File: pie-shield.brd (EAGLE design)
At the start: 35.1 x 25.2 mm, 20 parts, among them IC4 NRF24L01SMD, Q2 3.2X2.5CRYSTAL

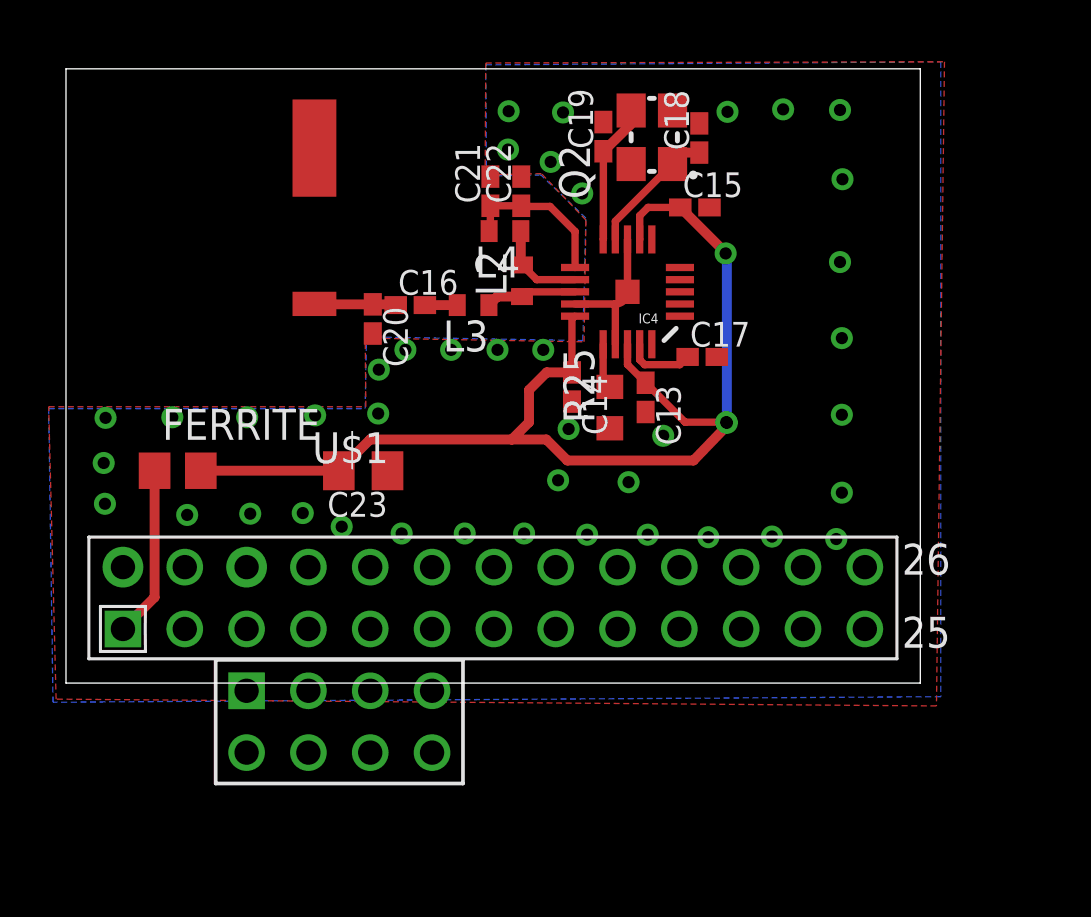
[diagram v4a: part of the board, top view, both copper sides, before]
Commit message: minified and dru tested
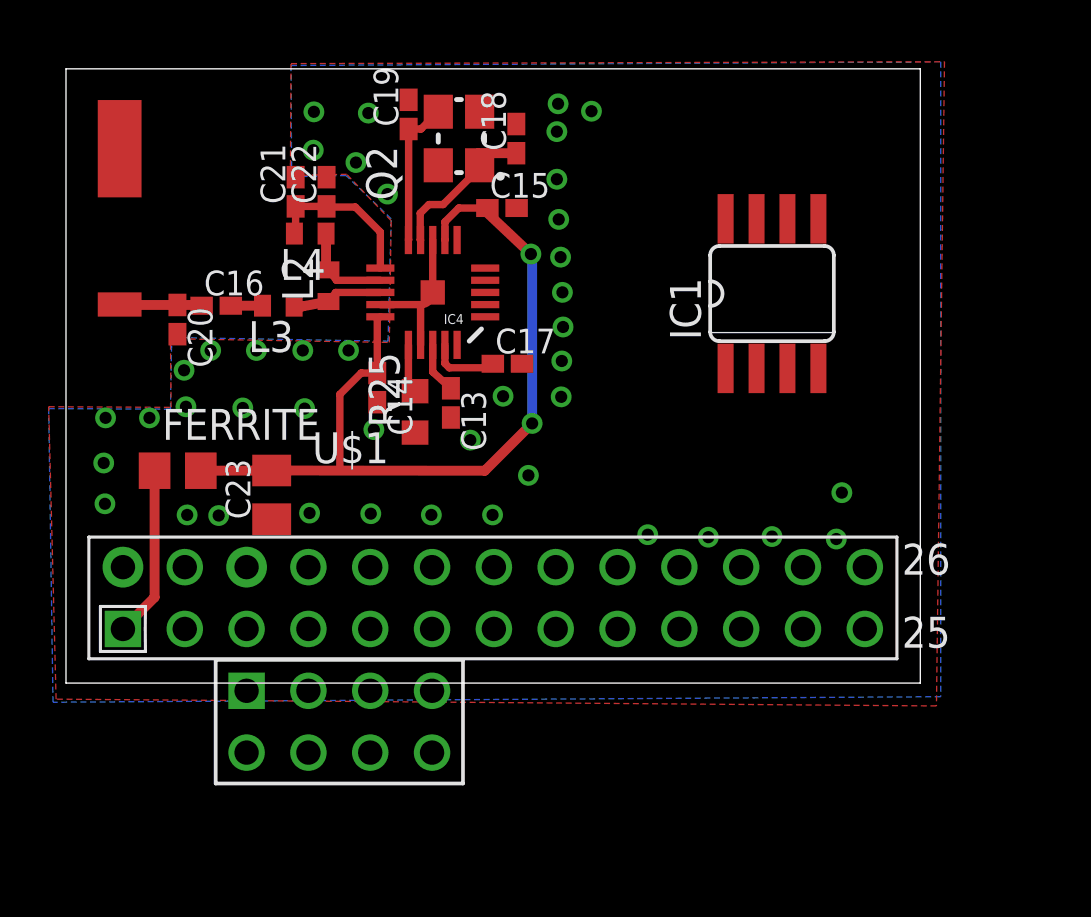
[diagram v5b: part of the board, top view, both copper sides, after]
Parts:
- added IC1: MAX481CSA, maxim:SO08
- moved C19 8.05 mm to (14.1, 25.0)
- moved C20 8.03 mm to (4.58, 16.6)
- moved C17 8.01 mm to (18.1, 14.8)
- moved C13 8.00 mm to (15.8, 13.2)
- moved R25 8.00 mm to (14.3, 12.8)
- moved L4 8.00 mm to (10.0, 20.1)
- moved C14 8.00 mm to (12.8, 13.8)
- moved C21 8.00 mm to (9.43, 21.9)
- moved ANT 8.00 mm to (2.21, 19.7)
- moved C22 8.00 mm to (10.7, 21.9)
- moved IC4 8.00 mm to (15.1, 17.7)
- moved L3 8.00 mm to (8.72, 17.2)
- moved C16 7.98 mm to (6.17, 17.2)
- moved L2 7.95 mm to (10.8, 18.0)
- moved Q2 7.92 mm to (16.1, 24.1)
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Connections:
- new net N$1: U$1.P1_25
- new net N$2: U$1.P1_26
- new net N$4: U$1.P1_24
- new net N$5: U$1.P1_22
- new net VCC: IC1.8
- net GND: now also IC1.5
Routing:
- net +3V3_RF: track 48.4 -> 39.1 mm, vias 3 -> 2
- net N$10: track 5.64 -> 6.51 mm
- net GND: vias 41 -> 42

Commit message: 1 square inch reached
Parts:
- removed IC1: MAX481CSA, maxim:SO08
- moved FERRITE 14.3 mm to (18.8, 8.98)
- moved C23 11.7 mm to (19.8, 12.0), turned to 270 degrees
- moved C15 10.1 mm to (28.0, 20.9)
- moved C17 10.1 mm to (28.3, 14.5)
- moved C21 10.1 mm to (19.6, 21.6)
- moved Q2 10.1 mm to (26.3, 23.7)
- moved C19 10.1 mm to (24.2, 24.7)
- moved C20 10.1 mm to (14.7, 16.3)
- moved C22 10.1 mm to (20.8, 21.6)
- moved IC4 10.1 mm to (25.2, 17.4)
- moved L2 10.1 mm to (20.9, 17.7)
- moved L3 10.1 mm to (18.9, 16.9)
- moved R25 10.1 mm to (24.5, 12.5)
- moved ANT 10.1 mm to (12.3, 19.4)
- moved C13 10.1 mm to (26.0, 12.9)
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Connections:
- removed net N$2: U$1.P1_26
- removed net N$5: U$1.P1_22
- removed net VCC: IC1.8
- net +3V3: now also U$1.P1_17; no longer U$1.P1_1
- net CE: now also U$1.P1_22
- net CSN: now also U$1.P1_24
- net GND: now also U$1.P1_25; no longer IC1.5
- net IRQ: now also U$1.P1_26
- net N$1: now also U$1.P1_15; no longer U$1.P1_25
- net N$3: now also U$1.P1_18; no longer U$1.P1_17
- net N$4: now also U$1.P1_16; no longer U$1.P1_24
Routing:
- net MOSI: track 0.00 -> 21.4 mm, vias 0 -> 1
- net MISO: track 0.00 -> 21.1 mm, vias 0 -> 1
- net IRQ: track 0.00 -> 19.3 mm
- net SCK: track 0.00 -> 17.5 mm
- net CSN: track 0.00 -> 13.1 mm
- net CE: track 0.00 -> 12.8 mm
- net +3V3: track 7.04 -> 8.24 mm
- net +3V3_RF: track 39.1 -> 38.6 mm
- net GND: vias 42 -> 32
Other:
- board size 35.1 x 25.2 mm -> 25 x 25.2 mm

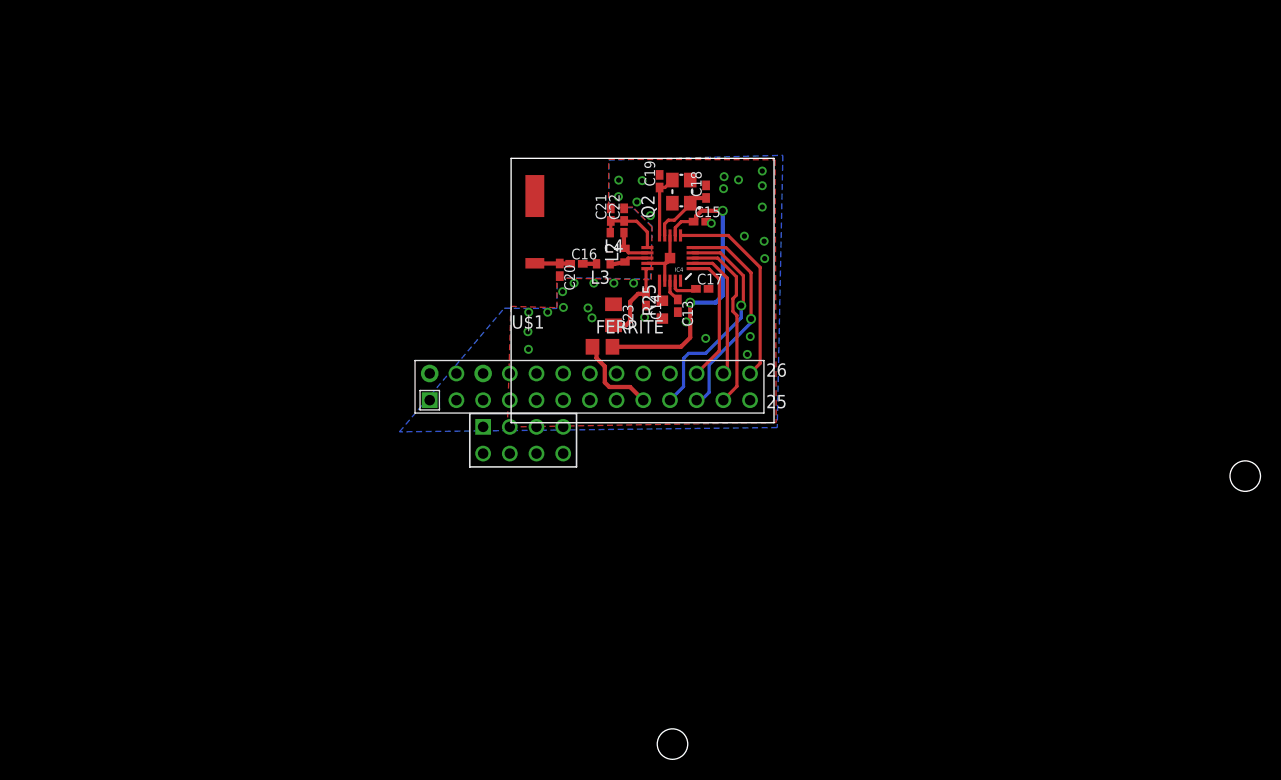
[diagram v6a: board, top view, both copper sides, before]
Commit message: fixed layout mirrored it
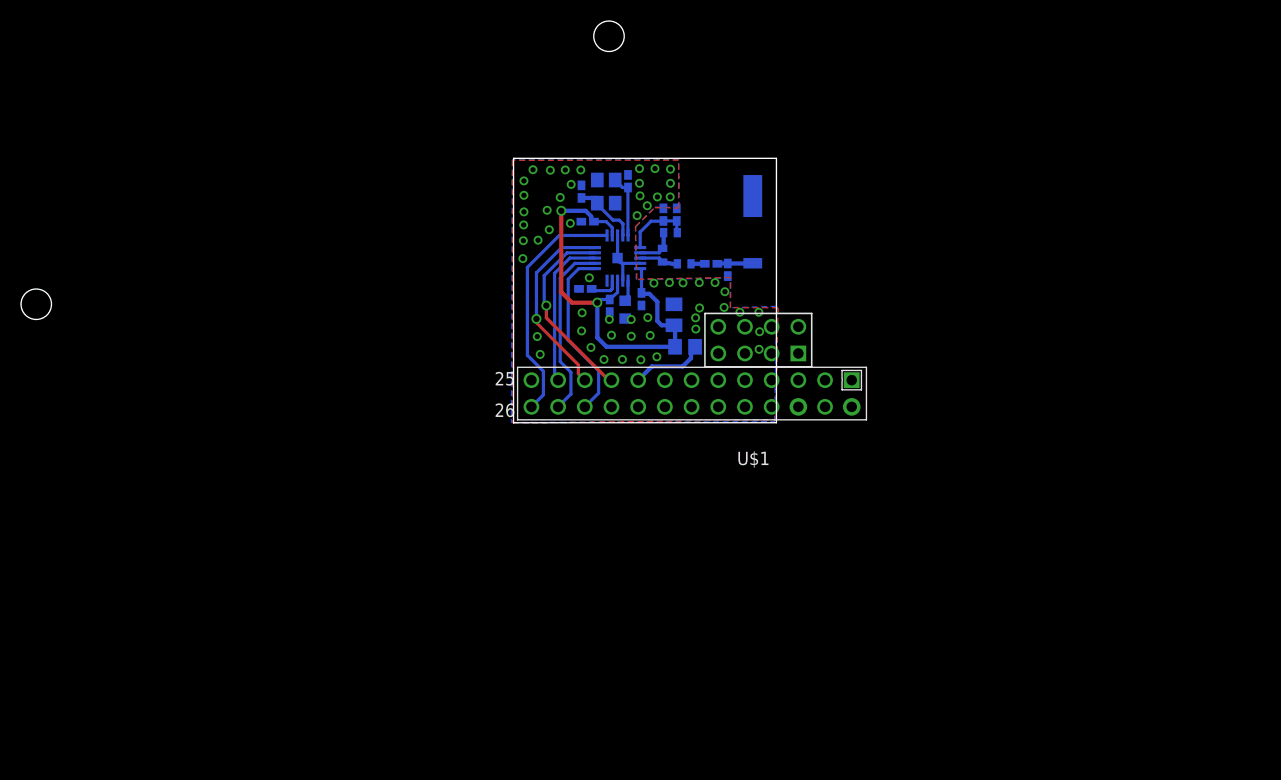
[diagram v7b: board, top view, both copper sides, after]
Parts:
- moved U$1 62.8 mm to (0.59, 27.4), turned to 180 degrees
- moved ANT 20.7 mm to (33.1, 19.4), flipped to the bottom
- moved C20 16.0 mm to (30.7, 16.3), flipped to the bottom
- moved C16 12.8 mm to (29.1, 16.9), flipped to the bottom
- moved C18 11.9 mm to (16.8, 23.7), flipped to the bottom
- moved C17 11.1 mm to (17.1, 14.5), flipped to the bottom
- moved C15 10.7 mm to (17.4, 20.9), flipped to the bottom
- moved FERRITE 7.86 mm to (26.6, 8.98), flipped to the bottom
- moved L3 7.70 mm to (26.6, 16.9), flipped to the bottom
- moved Q2 7.14 mm to (19.1, 23.7), flipped to the bottom
- moved C13 6.49 mm to (19.5, 12.9), flipped to the bottom
- moved C21 6.28 mm to (25.8, 21.6), flipped to the bottom
- moved C23 5.76 mm to (25.6, 12.0), flipped to the bottom
- moved L4 5.08 mm to (25.2, 19.8), flipped to the bottom
- moved IC4 4.99 mm to (20.2, 17.4), flipped to the bottom
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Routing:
- net CE: track 12.8 -> 16.9 mm
- net CSN: track 13.1 -> 17.1 mm
- net IRQ: track 19.3 -> 23.2 mm
- net +3V3_RF: track 38.6 -> 42.4 mm
- net MOSI: track 21.4 -> 18.5 mm
- net SCK: track 17.5 -> 14.7 mm
- net MISO: track 21.1 -> 18.7 mm
- net +3V3: track 8.24 -> 7.13 mm
- net GND: vias 32 -> 56

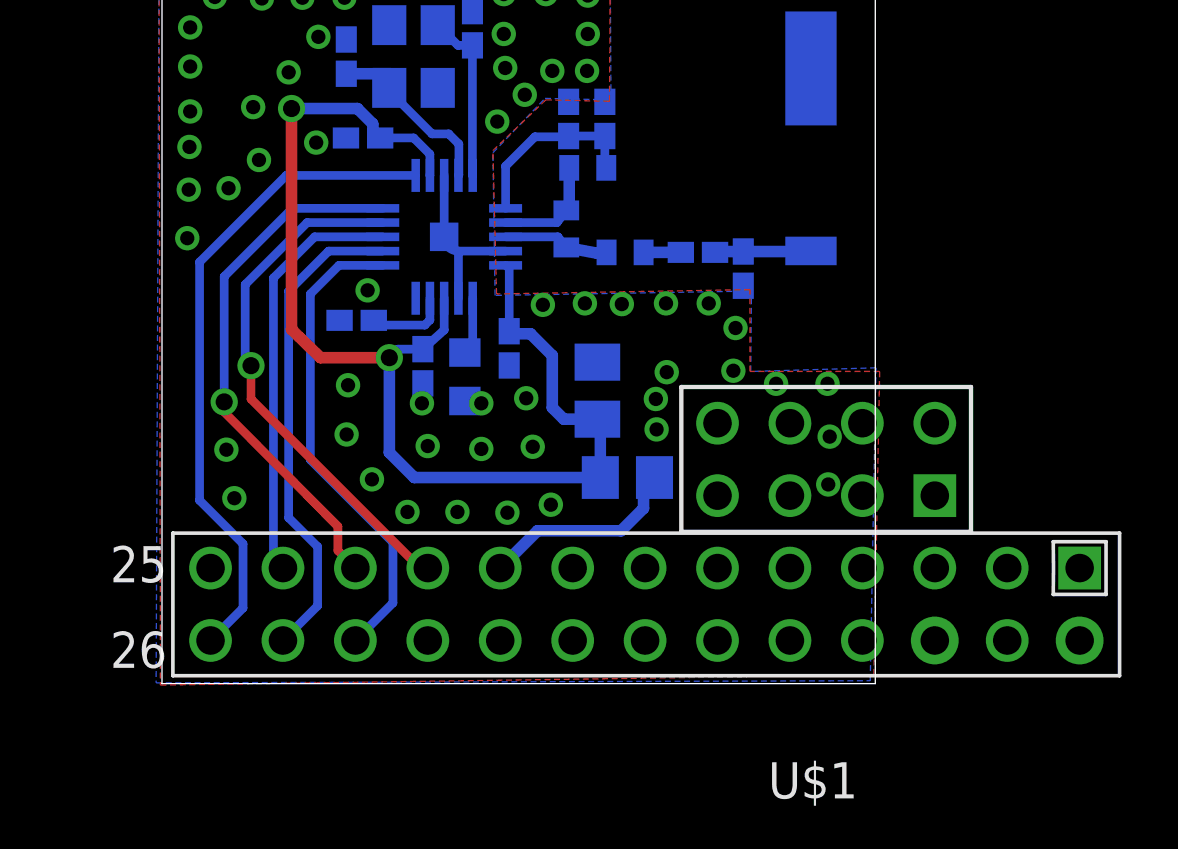
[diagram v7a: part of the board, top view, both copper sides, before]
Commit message: updated to smaller version of raspberry io
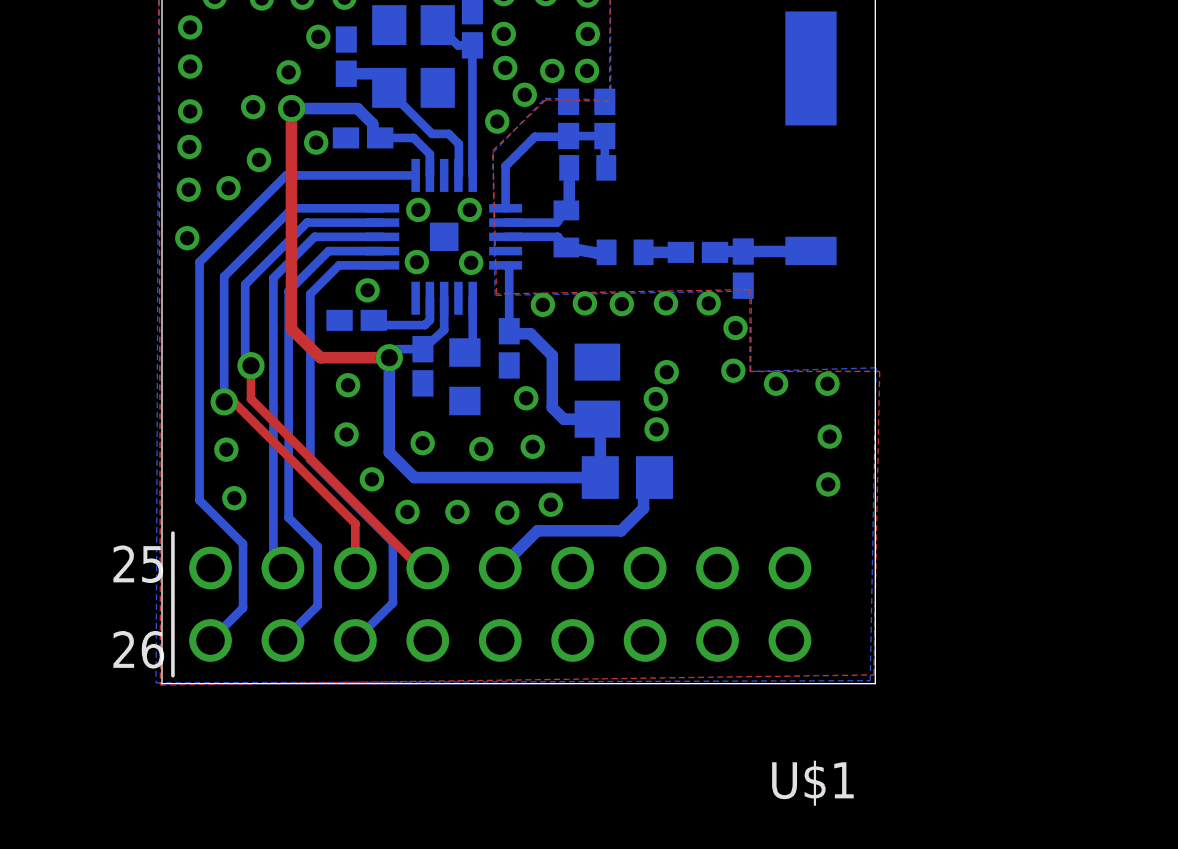
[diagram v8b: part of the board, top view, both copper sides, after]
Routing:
- net GND: track 6.17 -> 0.00 mm, vias 56 -> 58
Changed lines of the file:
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@@
 <layer number="27" name="tValues" color="7" fill="1" visible="yes" active="yes"/>
 <layer number="28" name="bValues" color="7" fill="1" visible="yes" active="yes"/>
-<layer number="29" name="tStop" color="7" fill="3" visible="no" active="yes"/>
-<layer number="30" name="bStop" color="7" fill="6" visible="no" active="yes"/>
+<layer number="29" name="tStop" color="7" fill="3" visible="yes" active="yes"/>
+<layer number="30" name="bStop" color="7" fill="6" visible="yes" active="yes"/>
 <layer number="31" name="tCream" color="7" fill="4" visible="no" active="yes"/>
 <layer number="32" name="bCream" color="7" fill="5" visible="no" active="yes"/>
@@
 <contactref element="U$1" pad="P1_14"/>
 <contactref element="U$1" pad="P1_9"/>
-<polygon width="0.3048" layer="16" orphans="yes" thermals="no">
+<polygon width="0.3048" layer="16" thermals="no">
 <vertex x="35.3568" y="12.827"/>
 <vertex x="30.9626" y="12.7"/>
@@
 <vertex x="35.1536" y="1.8542"/>
 </polygon>
-<polygon width="0.3048" layer="1">
+<polygon width="0.3048" layer="1" thermals="no">
 <vertex x="10.2616" y="1.7018"/>
 <vertex x="35.2806" y="2.0574"/>
@@
 <vertex x="10.2108" y="26.7208"/>
 </polygon>
-<wire x1="22.3656" y1="16.9206" x2="20.7116" y2="16.9206" width="0.3048" layer="16"/>
-<wire x1="20.7116" y1="16.9206" x2="20.2116" y2="17.4206" width="0.3048" layer="16" curve="-90"/>
-<wire x1="20.2116" y1="17.4206" x2="20.2116" y2="19.5746" width="0.3048" layer="16"/>
-<wire x1="20.7116" y1="15.2666" x2="20.7116" y2="16.9206" width="0.3048" layer="16"/>
 <via x="22.352" y="23.3426" extent="1-16" drill="0.5" shape="octagon"/>
 <via x="23.7744" y="25.9334" extent="1-16" drill="0.5" shape="octagon"/>
@@
 <via x="11.2522" y="19.0754" extent="1-16" drill="0.5" shape="octagon"/>
 <via x="16.8402" y="12.2174" extent="1-16" drill="0.5" shape="octagon"/>
-<via x="19.6342" y="10.0838" extent="1-16" drill="0.5" shape="octagon"/>
+<via x="19.4564" y="10.1854" extent="1-16" drill="0.5" shape="octagon"/>
 <via x="17.6784" y="8.9154" extent="1-16" drill="0.5" shape="octagon"/>
 <via x="18.923" y="7.7724" extent="1-16" drill="0.5" shape="octagon"/>
 <via x="20.6756" y="7.7724" extent="1-16" drill="0.5" shape="octagon"/>
 <via x="22.4282" y="7.747" extent="1-16" drill="0.5" shape="octagon"/>
-<via x="19.431" y="11.5824" extent="1-16" drill="0.5" shape="octagon"/>
 <via x="23.9522" y="8.0264" extent="1-16" drill="0.5" shape="octagon"/>
 <via x="21.5138" y="9.9822" extent="1-16" drill="0.5" shape="octagon"/>
@@
 <via x="17.526" y="15.5448" extent="1-16" drill="0.5" shape="octagon"/>
 <via x="23.3172" y="10.0584" extent="1-16" drill="0.5" shape="octagon"/>
-<via x="21.5138" y="11.5824" extent="1-16" drill="0.5" shape="octagon"/>
 <via x="27.6606" y="10.668" extent="1-16" drill="0.5" shape="octagon"/>
+<via x="19.304" y="18.3642" extent="1-16" drill="0.5" shape="octagon"/>
+<via x="19.2532" y="16.5354" extent="1-16" drill="0.5" shape="octagon"/>
+<via x="21.1582" y="16.51" extent="1-16" drill="0.5" shape="octagon"/>
+<via x="21.1074" y="18.3642" extent="1-16" drill="0.5" shape="octagon"/>
 </signal>
 <signal name="+3V3" class="2">
@@
 <wire x1="12.4968" y1="16.0274" x2="12.4968" y2="11.6332" width="0.3048" layer="16"/>
 <via x="12.4968" y="11.6332" extent="1-16" drill="0.6" shape="octagon"/>
-<wire x1="12.4968" y1="11.6332" x2="12.4968" y2="11.2776" width="0.3048" layer="1"/>
-<wire x1="12.4968" y1="11.2776" x2="16.4846" y2="7.2644" width="0.3048" layer="1"/>
-<wire x1="16.4846" y1="7.2644" x2="16.4846" y2="6.4178" width="0.3048" layer="1"/>
-<wire x1="16.4846" y1="6.4178" x2="17.0974" y2="5.805" width="0.3048" layer="1"/>
+<wire x1="12.4968" y1="11.6332" x2="12.827" y2="11.6332" width="0.3048" layer="1"/>
+<wire x1="12.827" y1="11.6332" x2="17.0974" y2="7.3628" width="0.3048" layer="1"/>
+<wire x1="17.0974" y1="7.3628" x2="17.0974" y2="5.805" width="0.3048" layer="1"/>
 </signal>
 <signal name="MOSI">
